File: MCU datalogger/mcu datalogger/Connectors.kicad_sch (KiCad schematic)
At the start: 4 parts, among them J1 Conn_01x04_Pin, J2 Conn_01x09_Pin, J3 Conn_01x04_Pin, J4 Conn_02x03_Odd_Even

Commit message: Completed the footprints association.
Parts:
- J1, J3: footprint (none) -> Connector_PinHeader_2.54mm:PinHeader_1x04_P2.54mm_Vertical
- J2: footprint (none) -> Connector_PinHeader_2.54mm:PinHeader_1x09_P2.54mm_Vertical
- J4: footprint (none) -> Connector_PinHeader_2.54mm:PinHeader_2x03_P2.54mm_Vertical
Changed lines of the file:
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@@
       (effects (font (size 1.27 1.27)))
     )
-    (property "Footprint" "" (at 149.86 68.58 0)
+    (property "Footprint" "Connector_PinHeader_2.54mm:PinHeader_1x04_P2.54mm_Vertical" (at 149.86 68.58 0)
       (effects (font (size 1.27 1.27)) hide)
     )
@@
       (effects (font (size 1.27 1.27)))
     )
-    (property "Footprint" "" (at 151.13 100.33 0)
+    (property "Footprint" "Connector_PinHeader_2.54mm:PinHeader_2x03_P2.54mm_Vertical" (at 151.13 100.33 0)
       (effects (font (size 1.27 1.27)) hide)
     )
@@
       (effects (font (size 1.27 1.27)))
     )
-    (property "Footprint" "" (at 125.73 68.58 0)
+    (property "Footprint" "Connector_PinHeader_2.54mm:PinHeader_1x04_P2.54mm_Vertical" (at 125.73 68.58 0)
       (effects (font (size 1.27 1.27)) hide)
     )
@@
       (effects (font (size 1.27 1.27)))
     )
-    (property "Footprint" "" (at 128.27 100.33 0)
+    (property "Footprint" "Connector_PinHeader_2.54mm:PinHeader_1x09_P2.54mm_Vertical" (at 128.27 100.33 0)
       (effects (font (size 1.27 1.27)) hide)
     )

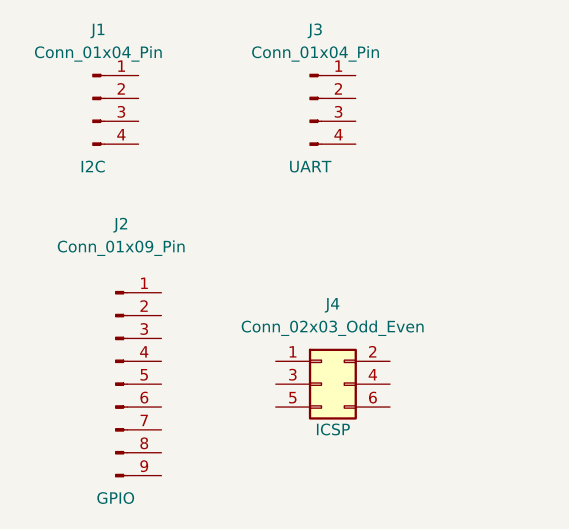
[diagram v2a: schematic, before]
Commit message: Completed wiring in the second sheet.
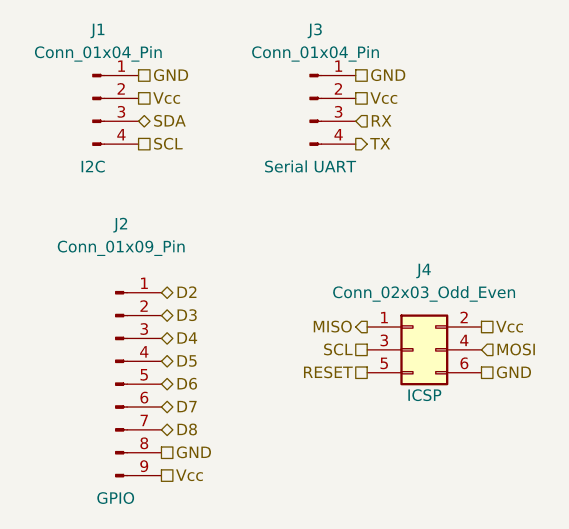
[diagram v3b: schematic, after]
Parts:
- J3: Purpose UART -> Serial UART
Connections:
- net GND: now reaches J3.1 (Pin_1)
- net GND: now also J1.1 (Pin_1), J2.8 (Pin_8), J4.6 (Pin_6)
- net Vcc: now reaches J3.2 (Pin_2)
- net Vcc: now also J1.2 (Pin_2), J2.9 (Pin_9), J4.2 (Pin_2)
- net RX: now reaches J3.3 (Pin_3)
- net TX: now reaches J3.4 (Pin_4)
- net MISO: now reaches J4.1 (Pin_1)
- net SCL: now reaches J4.3 (Pin_3)
- net SCL: now also J1.4 (Pin_4)
- net MOSI: now reaches J4.4 (Pin_4)
- net RESET: now reaches J4.5 (Pin_5)
- net SDA: now reaches J1.3 (Pin_3)
- net D2: now reaches J2.1 (Pin_1)
- net D3: now reaches J2.2 (Pin_2)
- net D4: now reaches J2.3 (Pin_3)
- net D5: now reaches J2.4 (Pin_4)
- net D6: now reaches J2.5 (Pin_5)
- net D7: now reaches J2.6 (Pin_6)
- net D8: now reaches J2.7 (Pin_7)
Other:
- moved on the sheet: J4
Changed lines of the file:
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@@
 (kicad_sch (version 20230121) (generator eeschema)
   (paper "A4")
+  (hierarchical_label "D3" (shape bidirectional) (at 133.35 92.71 0) (fields_autoplaced)
+    (effects (font (size 1.27 1.27)) (justify left))
+  )
+  (hierarchical_label "D6" (shape bidirectional) (at 133.35 100.33 0) (fields_autoplaced)
+    (effects (font (size 1.27 1.27)) (justify left))
+  )
+  (hierarchical_label "Vcc" (shape passive) (at 133.35 110.49 0) (fields_autoplaced)
+    (effects (font (size 1.27 1.27)) (justify left))
+  )
+  (hierarchical_label "GND" (shape passive) (at 154.94 66.04 0) (fields_autoplaced)
+    (effects (font (size 1.27 1.27)) (justify left))
+  )
+  (hierarchical_label "Vcc" (shape passive) (at 130.81 68.58 0) (fields_autoplaced)
+    (effects (font (size 1.27 1.27)) (justify left))
+  )
+  (hierarchical_label "GND" (shape passive) (at 133.35 107.95 0) (fields_autoplaced)
+    (effects (font (size 1.27 1.27)) (justify left))
+  )
+  (hierarchical_label "D5" (shape bidirectional) (at 133.35 97.79 0) (fields_autoplaced)
+    (effects (font (size 1.27 1.27)) (justify left))
+  )
+  (hierarchical_label "D7" (shape bidirectional) (at 133.35 102.87 0) (fields_autoplaced)
+    (effects (font (size 1.27 1.27)) (justify left))
+  )
+  (hierarchical_label "SCL" (shape passive) (at 156.21 96.52 180) (fields_autoplaced)
+    (effects (font (size 1.27 1.27)) (justify right))
+  )
+  (hierarchical_label "D2" (shape bidirectional) (at 133.35 90.17 0) (fields_autoplaced)
+    (effects (font (size 1.27 1.27)) (justify left))
+  )
+  (hierarchical_label "GND" (shape passive) (at 168.91 99.06 0) (fields_autoplaced)
+    (effects (font (size 1.27 1.27)) (justify left))
+  )
+  (hierarchical_label "TX" (shape output) (at 154.94 73.66 0) (fields_autoplaced)
+    (effects (font (size 1.27 1.27)) (justify left))
+  )
+  (hierarchical_label "Vcc" (shape passive) (at 168.91 93.98 0) (fields_autoplaced)
+    (effects (font (size 1.27 1.27)) (justify left))
+  )
+  (hierarchical_label "D4" (shape bidirectional) (at 133.35 95.25 0) (fields_autoplaced)
+    (effects (font (size 1.27 1.27)) (justify left))
+  )
+  (hierarchical_label "D8" (shape bidirectional) (at 133.35 105.41 0) (fields_autoplaced)
+    (effects (font (size 1.27 1.27)) (justify left))
+  )
+  (hierarchical_label "RX" (shape input) (at 154.94 71.12 0) (fields_autoplaced)
+    (effects (font (size 1.27 1.27)) (justify left))
+  )
+  (hierarchical_label "SDA" (shape bidirectional) (at 130.81 71.12 0) (fields_autoplaced)
+    (effects (font (size 1.27 1.27)) (justify left))
+  )
+  (hierarchical_label "Vcc" (shape passive) (at 154.94 68.58 0) (fields_autoplaced)
+    (effects (font (size 1.27 1.27)) (justify left))
+  )
+  (hierarchical_label "GND" (shape passive) (at 130.81 66.04 0) (fields_autoplaced)
+    (effects (font (size 1.27 1.27)) (justify left))
+  )
+  (hierarchical_label "MISO" (shape output) (at 156.21 93.98 180) (fields_autoplaced)
+    (effects (font (size 1.27 1.27)) (justify right))
+  )
+  (hierarchical_label "RESET" (shape passive) (at 156.21 99.06 180) (fields_autoplaced)
+    (effects (font (size 1.27 1.27)) (justify right))
+  )
+  (hierarchical_label "SCL" (shape passive) (at 130.81 73.66 0) (fields_autoplaced)
+    (effects (font (size 1.27 1.27)) (justify left))
+  )
+  (hierarchical_label "MOSI" (shape input) (at 168.91 96.52 0) (fields_autoplaced)
+    (effects (font (size 1.27 1.27)) (justify left))
+  )
   (symbol (lib_id "Connector:Conn_01x04_Pin") (at 149.86 68.58 0) (unit 1)
     (in_bom yes) (on_board yes) (dnp no)
@@
       (effects (font (size 1.27 1.27)) hide)
     )
-    (property "Purpose" "UART" (at 149.86 76.2 0)
+    (property "Purpose" "Serial UART" (at 149.86 76.2 0)
       (effects (font (size 1.27 1.27)))
     )
@@
     )
   )
-  (symbol (lib_id "Connector_Generic:Conn_02x03_Odd_Even") (at 151.13 100.33 0) (unit 1)
+  (symbol (lib_id "Connector_Generic:Conn_02x03_Odd_Even") (at 161.29 96.52 0) (unit 1)
     (in_bom yes) (on_board yes) (dnp no)
-    (property "Reference" "J4" (at 152.4 91.44 0)
+    (property "Reference" "J4" (at 162.56 87.63 0)
       (effects (font (size 1.27 1.27)))
     )
-    (property "Value" "Conn_02x03_Odd_Even" (at 152.4 93.98 0)
+    (property "Value" "Conn_02x03_Odd_Even" (at 162.56 90.17 0)
       (effects (font (size 1.27 1.27)))
     )
-    (property "Footprint" "Connector_PinHeader_2.54mm:PinHeader_2x03_P2.54mm_Vertical" (at 151.13 100.33 0)
+    (property "Footprint" "Connector_PinHeader_2.54mm:PinHeader_2x03_P2.54mm_Vertical" (at 161.29 96.52 0)
       (effects (font (size 1.27 1.27)) hide)
     )
-    (property "Datasheet" "~" (at 151.13 100.33 0)
+    (property "Datasheet" "~" (at 161.29 96.52 0)
       (effects (font (size 1.27 1.27)) hide)
     )
-    (property "Purpose" "ICSP" (at 152.4 105.41 0)
+    (property "Purpose" "ICSP" (at 162.56 101.6 0)
       (effects (font (size 1.27 1.27)))
     )

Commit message: Completed 2 layer PCB project.
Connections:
- net SCL: no longer J4.3 (Pin_3)
- new net SCK: J4.3 (Pin_3)
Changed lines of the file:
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@@
     (effects (font (size 1.27 1.27)) (justify left))
   )
-  (hierarchical_label "SCL" (shape passive) (at 156.21 96.52 180) (fields_autoplaced)
+  (hierarchical_label "SCK" (shape passive) (at 156.21 96.52 180) (fields_autoplaced)
     (effects (font (size 1.27 1.27)) (justify right))
   )
